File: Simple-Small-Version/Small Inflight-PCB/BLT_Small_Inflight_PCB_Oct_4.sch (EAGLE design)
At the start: 7 parts

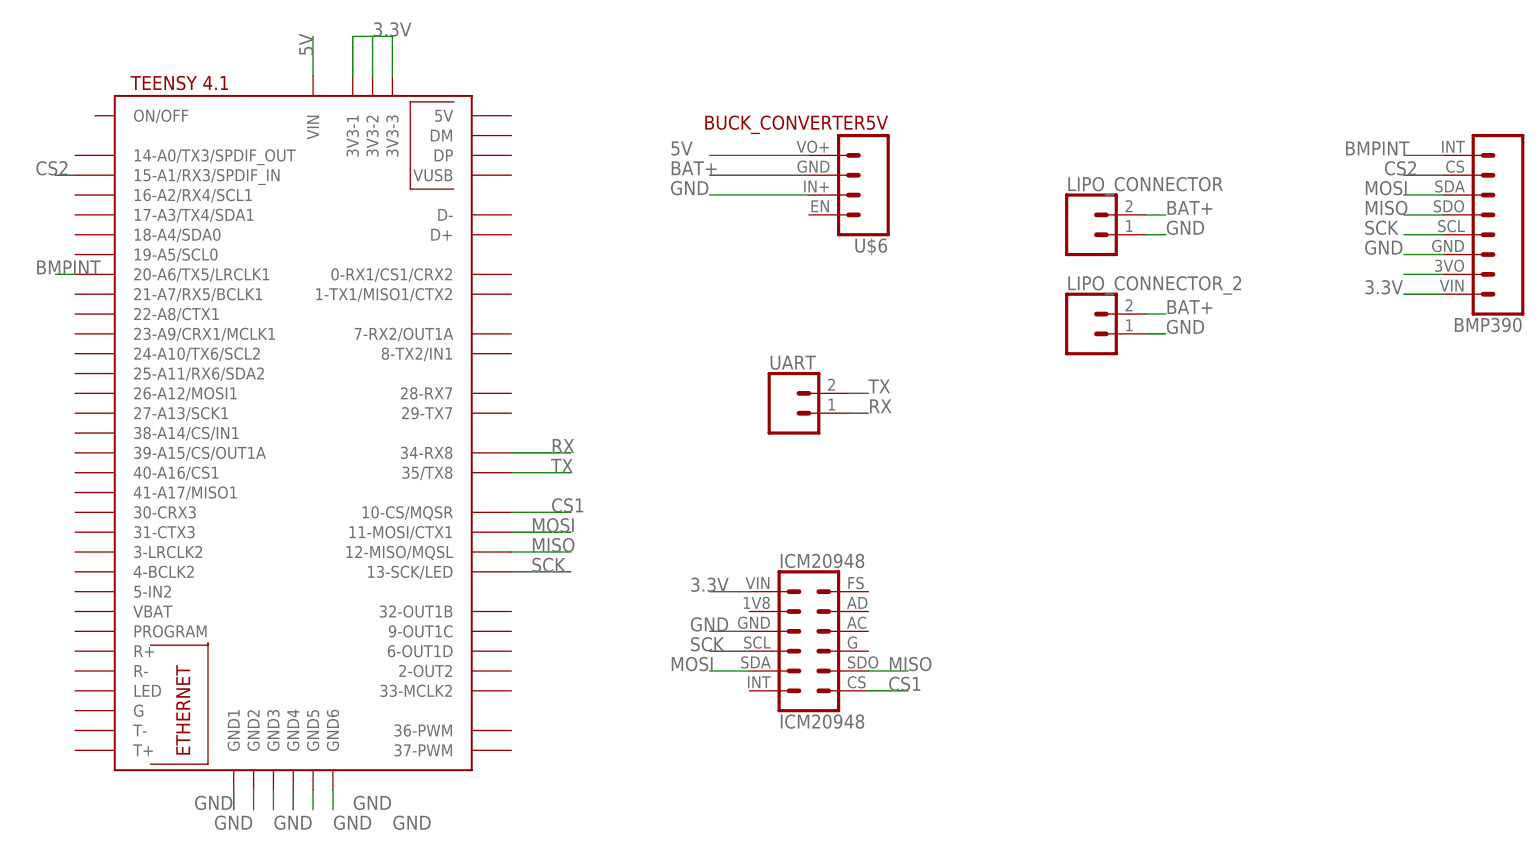
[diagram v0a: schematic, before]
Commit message: Updated layout
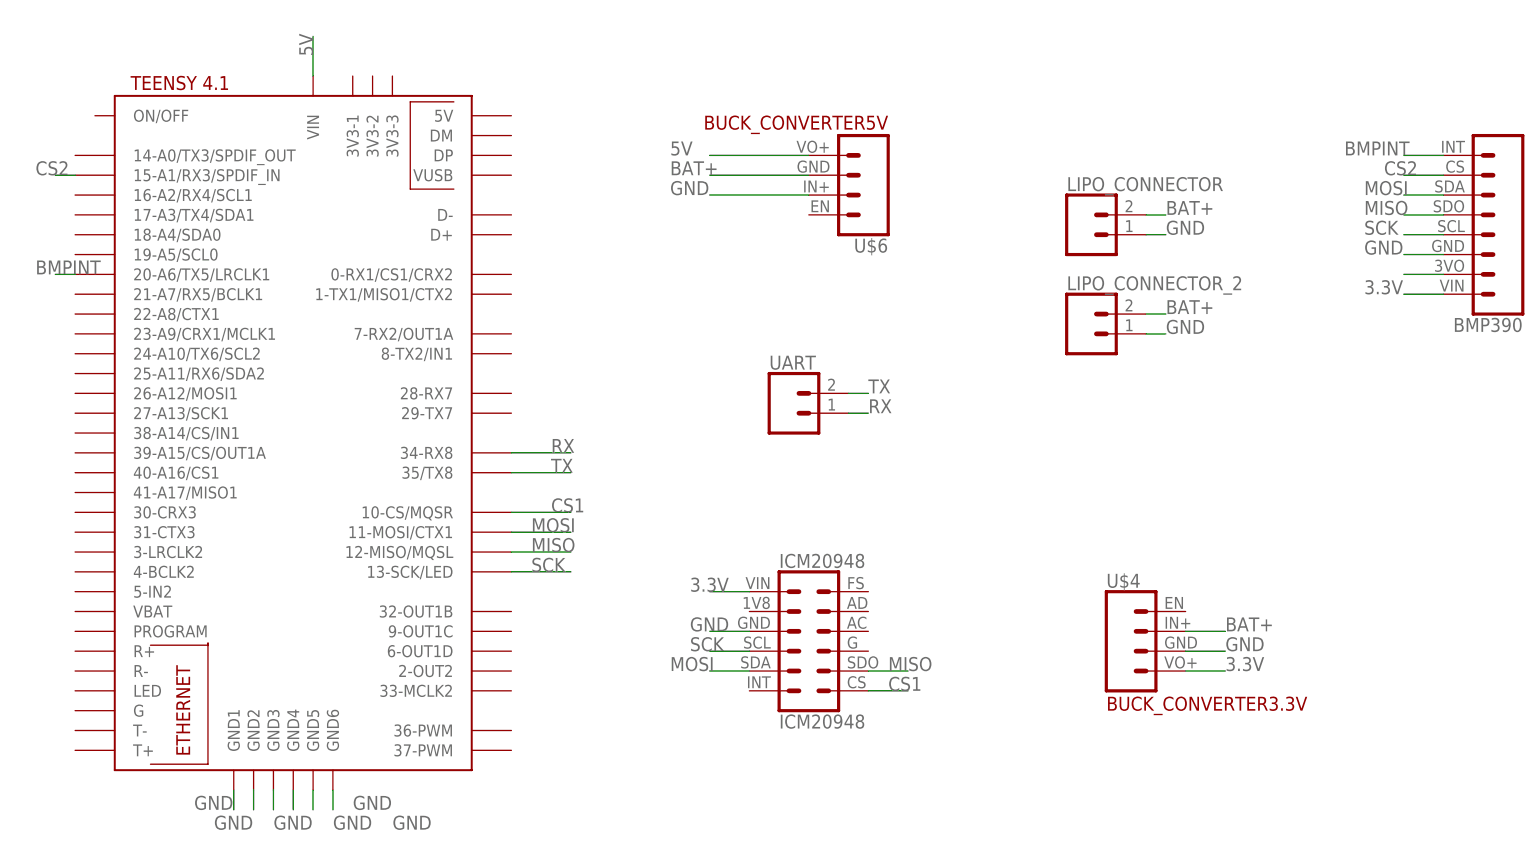
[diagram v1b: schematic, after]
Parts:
- added U$4: BUCK_CONVERTER3.3V, BLTFootprints:BUCK_CONVERTER3.3V
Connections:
- removed net N$3: U$1.3V3-1, U$1.3V3-3
- net 3.3V: now also U$4.VO+; no longer U$1.3V3-2
- net BAT+: now also U$4.IN+
- net GND: now also U$4.GND
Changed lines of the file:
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@@
 <drawing>
 <settings>
-<setting alwaysvectorfont="no"/>
+<setting alwaysvectorfont="yes"/>
 <setting verticaltext="up"/>
 </settings>
@@
 <part name="U$3" library="ICM20948" deviceset="ICM20948" device=""/>
 <part name="UART" library="SparkFun-Connectors" library_urn="urn:adsk.eagle:library:513" deviceset="CONN_02" device="" package3d_urn="urn:adsk.eagle:package:38039/1"/>
+<part name="U$4" library="BLTFootprints" deviceset="BUCK_CONVERTER" device="" technology="3.3V"/>
 </parts>
 <sheets>
@@
 <attribute name="NAME" x="111.76" y="48.768" size="1.778" layer="95" font="vector"/>
 </instance>
+<instance part="U$4" gate="G$1" x="160.02" y="12.7" smashed="yes">
+<attribute name="NAME" x="154.94" y="20.828" size="1.778" layer="95" font="vector"/>
+<attribute name="VALUE" x="154.94" y="5.08" size="1.778" layer="94"/>
+</instance>
 </instances>
 <busses>
@@
 </segment>
 <segment>
-<pinref part="U$1" gate="G$1" pin="3V3-2"/>
-<wire x1="60.96" y1="86.36" x2="60.96" y2="91.44" width="0.1524" layer="91"/>
-<label x="60.96" y="91.44" size="1.778" layer="95"/>
-</segment>
-<segment>
 <pinref part="U$3" gate="G$1" pin="VIN"/>
 <wire x1="109.22" y1="20.32" x2="104.14" y2="20.32" width="0.1524" layer="91"/>
 <label x="101.6" y="20.32" size="1.778" layer="95"/>
 </segment>
+<segment>
+<pinref part="U$4" gate="G$1" pin="VO+"/>
+<wire x1="165.1" y1="10.16" x2="170.18" y2="10.16" width="0.1524" layer="91"/>
+<label x="170.18" y="10.16" size="1.778" layer="95"/>
+</segment>
 </net>
 <net name="GND" class="0">
@@
 <label x="101.6" y="15.24" size="1.778" layer="95"/>
 </segment>
+<segment>
+<pinref part="U$4" gate="G$1" pin="GND"/>
+<wire x1="165.1" y1="12.7" x2="170.18" y2="12.7" width="0.1524" layer="91"/>
+<label x="170.18" y="12.7" size="1.778" layer="95"/>
+</segment>
 </net>
 <net name="SCK" class="0">
@@
 <label x="162.56" y="55.88" size="1.778" layer="95"/>
 </segment>
+<segment>
+<pinref part="U$4" gate="G$1" pin="IN+"/>
+<wire x1="165.1" y1="15.24" x2="170.18" y2="15.24" width="0.1524" layer="91"/>
+<label x="170.18" y="15.24" size="1.778" layer="95"/>
+</segment>
 </net>
 <net name="BMPINT" class="0">
@@
 </segment>
 </net>
-<net name="N$3" class="0">
-<segment>
-<pinref part="U$1" gate="G$1" pin="3V3-3"/>
-<wire x1="63.5" y1="86.36" x2="63.5" y2="91.44" width="0.1524" layer="91"/>
-<pinref part="U$1" gate="G$1" pin="3V3-1"/>
-<wire x1="58.42" y1="86.36" x2="58.42" y2="91.44" width="0.1524" layer="91"/>
-<wire x1="63.5" y1="91.44" x2="58.42" y2="91.44" width="0.1524" layer="91"/>
-</segment>
-</net>

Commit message: Updated files
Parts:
- removed LIPO_CONNECTOR: (no value), SparkFun-Connectors:CONN_02PTH4
- removed U$4: BUCK_CONVERTER3.3V, BLTFootprints:BUCK_CONVERTER3.3V
- added J1: (no value), SparkFun-Connectors:CONN_02PTH4
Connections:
- net 3.3V: now also U$1.3V3-1, U$1.3V3-3; no longer U$4.VO+
- net BAT+: now also J1.2; no longer LIPO_CONNECTOR.2, U$4.IN+
- net BMPINT: now also U$1.3-LRCLK2; no longer U$1.20-A6/TX5/LRCLK1
- net CS2: now also U$1.4-BCLK2; no longer U$1.15-A1/RX3/SPDIF_IN
- net GND: now also J1.1; no longer LIPO_CONNECTOR.1, U$4.GND
- net RX: now also U$1.0-RX1/CS1/CRX2; no longer U$1.34-RX8
- net TX: now also U$1.1-TX1/MISO1/CTX2; no longer U$1.35/TX8
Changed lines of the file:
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@@
 <part name="U$6" library="BLTFootprints" deviceset="BUCK_CONVERTER" device="" technology="5V"/>
 <part name="U$2" library="BLTFootprints" deviceset="BMP390" device=""/>
-<part name="LIPO_CONNECTOR" library="SparkFun-Connectors" library_urn="urn:adsk.eagle:library:513" deviceset="CONN_02" device="PTH4" package3d_urn="urn:adsk.eagle:package:38054/1"/>
 <part name="LIPO_CONNECTOR_2" library="SparkFun-Connectors" library_urn="urn:adsk.eagle:library:513" deviceset="CONN_02" device="" package3d_urn="urn:adsk.eagle:package:38039/1"/>
 <part name="U$3" library="ICM20948" deviceset="ICM20948" device=""/>
 <part name="UART" library="SparkFun-Connectors" library_urn="urn:adsk.eagle:library:513" deviceset="CONN_02" device="" package3d_urn="urn:adsk.eagle:package:38039/1"/>
-<part name="U$4" library="BLTFootprints" deviceset="BUCK_CONVERTER" device="" technology="3.3V"/>
+<part name="J1" library="SparkFun-Connectors" library_urn="urn:adsk.eagle:library:513" deviceset="CONN_02" device="PTH4" package3d_urn="urn:adsk.eagle:package:38054/1"/>
 </parts>
 <sheets>
@@
 </instance>
 <instance part="U$2" gate="G$1" x="203.2" y="68.58" smashed="yes" rot="R180"/>
-<instance part="LIPO_CONNECTOR" gate="G$1" x="152.4" y="66.04" smashed="yes">
-<attribute name="VALUE" x="149.86" y="61.214" size="1.778" layer="96" font="vector"/>
-<attribute name="NAME" x="149.86" y="71.628" size="1.778" layer="95" font="vector"/>
-</instance>
 <instance part="LIPO_CONNECTOR_2" gate="G$1" x="152.4" y="53.34" smashed="yes">
 <attribute name="VALUE" x="149.86" y="48.514" size="1.778" layer="96" font="vector"/>
@@
 <attribute name="NAME" x="111.76" y="48.768" size="1.778" layer="95" font="vector"/>
 </instance>
-<instance part="U$4" gate="G$1" x="160.02" y="12.7" smashed="yes">
-<attribute name="NAME" x="154.94" y="20.828" size="1.778" layer="95" font="vector"/>
-<attribute name="VALUE" x="154.94" y="5.08" size="1.778" layer="94"/>
+<instance part="J1" gate="G$1" x="152.4" y="68.58" smashed="yes">
+<attribute name="VALUE" x="149.86" y="63.754" size="1.778" layer="96" font="vector"/>
+<attribute name="NAME" x="149.86" y="74.168" size="1.778" layer="95" font="vector"/>
 </instance>
 </instances>
@@
 </segment>
 <segment>
-<pinref part="U$4" gate="G$1" pin="VO+"/>
-<wire x1="165.1" y1="10.16" x2="170.18" y2="10.16" width="0.1524" layer="91"/>
-<label x="170.18" y="10.16" size="1.778" layer="95"/>
+<pinref part="U$1" gate="G$1" pin="3V3-1"/>
+<wire x1="58.42" y1="86.36" x2="58.42" y2="91.44" width="0.1524" layer="91"/>
+<pinref part="U$1" gate="G$1" pin="3V3-3"/>
+<wire x1="58.42" y1="91.44" x2="63.5" y2="91.44" width="0.1524" layer="91"/>
+<wire x1="63.5" y1="91.44" x2="63.5" y2="86.36" width="0.1524" layer="91"/>
+<label x="63.5" y="91.44" size="1.778" layer="95"/>
 </segment>
 </net>
@@
 </segment>
 <segment>
-<pinref part="LIPO_CONNECTOR" gate="G$1" pin="1"/>
-<wire x1="160.02" y1="66.04" x2="162.56" y2="66.04" width="0.1524" layer="91"/>
-<label x="162.56" y="66.04" size="1.778" layer="95"/>
-</segment>
-<segment>
 <pinref part="LIPO_CONNECTOR_2" gate="G$1" pin="1"/>
 <wire x1="160.02" y1="53.34" x2="162.56" y2="53.34" width="0.1524" layer="91"/>
@@
 </segment>
 <segment>
-<pinref part="U$4" gate="G$1" pin="GND"/>
-<wire x1="165.1" y1="12.7" x2="170.18" y2="12.7" width="0.1524" layer="91"/>
-<label x="170.18" y="12.7" size="1.778" layer="95"/>
+<pinref part="J1" gate="G$1" pin="1"/>
+<wire x1="160.02" y1="68.58" x2="167.64" y2="68.58" width="0.1524" layer="91"/>
+<label x="160.02" y="68.58" size="1.778" layer="95"/>
 </segment>
 </net>
@@
 </segment>
 <segment>
-<pinref part="LIPO_CONNECTOR" gate="G$1" pin="2"/>
-<wire x1="160.02" y1="68.58" x2="162.56" y2="68.58" width="0.1524" layer="91"/>
-<label x="162.56" y="68.58" size="1.778" layer="95"/>
-</segment>
-<segment>
 <pinref part="LIPO_CONNECTOR_2" gate="G$1" pin="2"/>
 <wire x1="160.02" y1="55.88" x2="162.56" y2="55.88" width="0.1524" layer="91"/>
@@
 </segment>
 <segment>
-<pinref part="U$4" gate="G$1" pin="IN+"/>
-<wire x1="165.1" y1="15.24" x2="170.18" y2="15.24" width="0.1524" layer="91"/>
-<label x="170.18" y="15.24" size="1.778" layer="95"/>
+<pinref part="J1" gate="G$1" pin="2"/>
+<wire x1="160.02" y1="71.12" x2="167.64" y2="71.12" width="0.1524" layer="91"/>
+<label x="160.02" y="71.12" size="1.778" layer="95"/>
 </segment>
 </net>
 <net name="BMPINT" class="0">
-<segment>
-<pinref part="U$1" gate="G$1" pin="20-A6/TX5/LRCLK1"/>
-<wire x1="22.86" y1="60.96" x2="20.32" y2="60.96" width="0.1524" layer="91"/>
-<label x="17.78" y="60.96" size="1.778" layer="95"/>
-</segment>
 <segment>
 <wire x1="198.12" y1="76.2" x2="193.04" y2="76.2" width="0.1524" layer="91"/>
@@
 <pinref part="U$2" gate="G$1" pin="INT"/>
 </segment>
+<segment>
+<pinref part="U$1" gate="G$1" pin="3-LRCLK2"/>
+<wire x1="22.86" y1="25.4" x2="17.78" y2="25.4" width="0.1524" layer="91"/>
+<label x="15.24" y="25.4" size="1.778" layer="95"/>
+</segment>
 </net>
 <net name="N$13" class="0">
@@
 </net>
 <net name="CS2" class="0">
-<segment>
-<pinref part="U$1" gate="G$1" pin="15-A1/RX3/SPDIF_IN"/>
-<wire x1="22.86" y1="73.66" x2="20.32" y2="73.66" width="0.1524" layer="91"/>
-<label x="17.78" y="73.66" size="1.778" layer="95"/>
-</segment>
 <segment>
 <wire x1="198.12" y1="73.66" x2="193.04" y2="73.66" width="0.1524" layer="91"/>
@@
 <pinref part="U$2" gate="G$1" pin="CS"/>
 </segment>
+<segment>
+<pinref part="U$1" gate="G$1" pin="4-BCLK2"/>
+<wire x1="22.86" y1="22.86" x2="17.78" y2="22.86" width="0.1524" layer="91"/>
+<label x="17.78" y="22.86" size="1.778" layer="95"/>
+</segment>
 </net>
 <net name="TX" class="0">
@@
 </segment>
 <segment>
-<pinref part="U$1" gate="G$1" pin="35/TX8"/>
-<wire x1="78.74" y1="35.56" x2="86.36" y2="35.56" width="0.1524" layer="91"/>
-<label x="83.82" y="35.56" size="1.778" layer="95"/>
+<wire x1="78.74" y1="58.42" x2="86.36" y2="58.42" width="0.1524" layer="91"/>
+<label x="83.82" y="58.42" size="1.778" layer="95"/>
+<pinref part="U$1" gate="G$1" pin="1-TX1/MISO1/CTX2"/>
 </segment>
 </net>
@@
 </segment>
 <segment>
-<pinref part="U$1" gate="G$1" pin="34-RX8"/>
-<wire x1="78.74" y1="38.1" x2="86.36" y2="38.1" width="0.1524" layer="91"/>
-<label x="83.82" y="38.1" size="1.778" layer="95"/>
-</segment>
-</net>
+<wire x1="78.74" y1="60.96" x2="86.36" y2="60.96" width="0.1524" layer="91"/>
+<label x="83.82" y="60.96" size="1.778" layer="95"/>
+<pinref part="U$1" gate="G$1" pin="0-RX1/CS1/CRX2"/>
+</segment>
+</net>
